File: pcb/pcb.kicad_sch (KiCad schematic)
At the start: 37 parts, among them J1 Ribbon Cable Header, J2 Ribbon Cable Header, J3 UPDI, SW1 MX Grey w/ LED, SW2 MX Grey w/ LED, SW3 1241.1100.7095, SW4 SW_SPST, U1 Display Driver, U2 Display Driver, U3 MCU, U4 OR, 2 Channels, U5 5V Buck Voltage Regulator, Y1 32.768 kHz

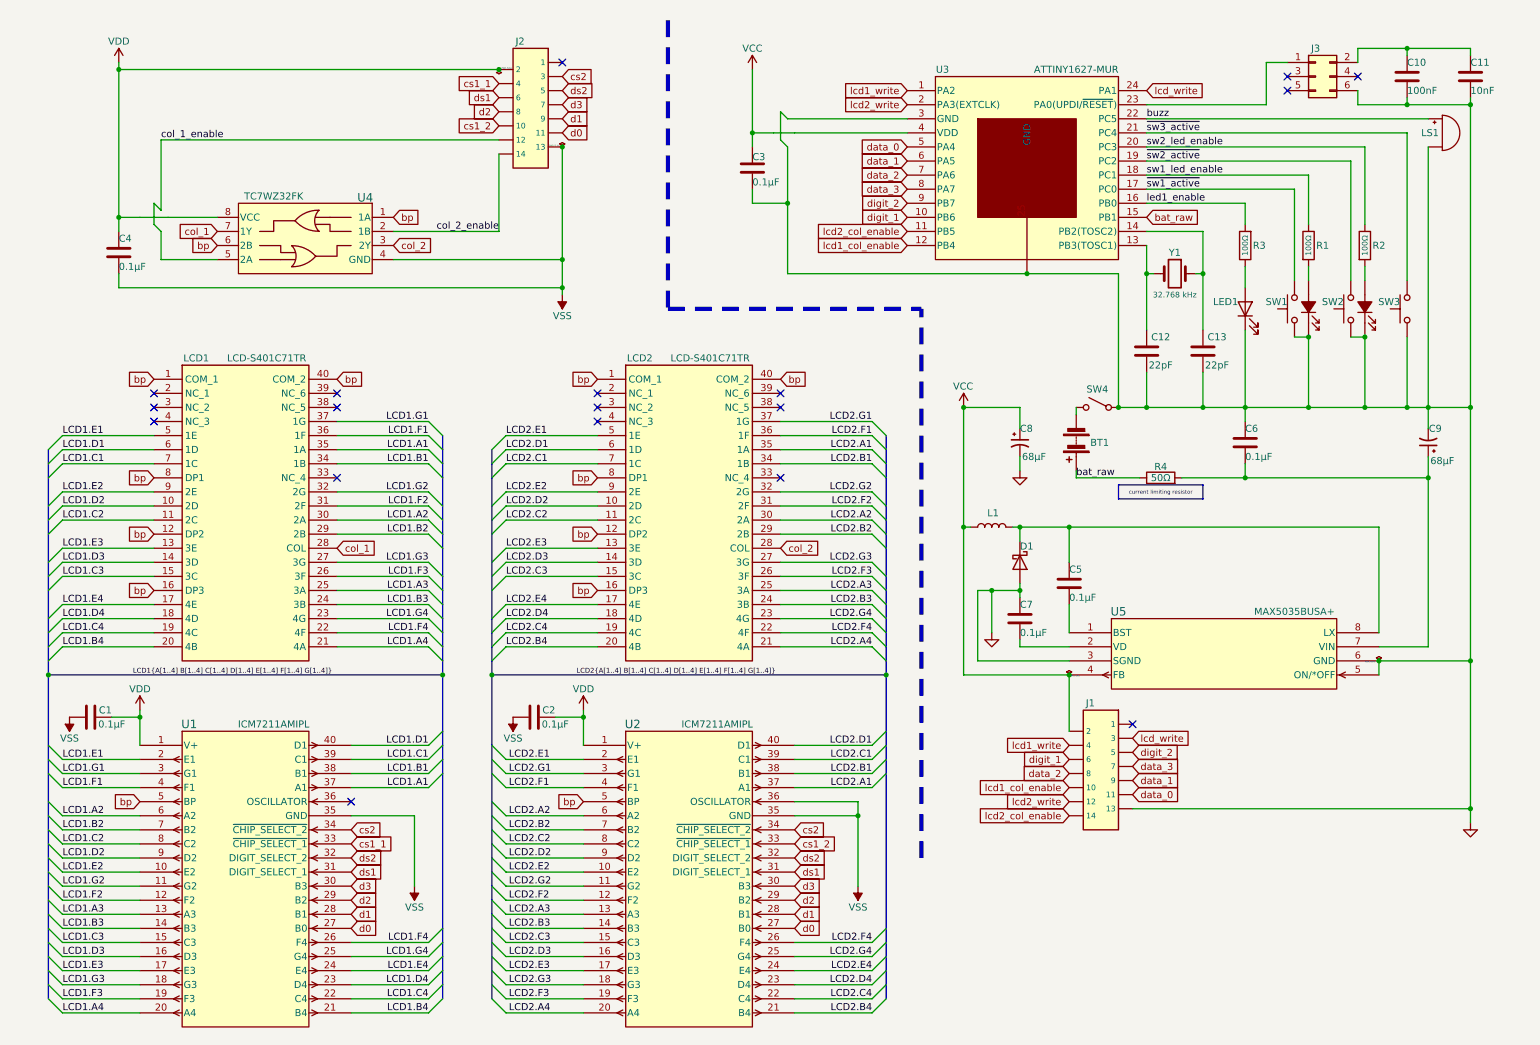
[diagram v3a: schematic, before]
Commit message: standardize cross-connector net names
Signed-off-by: Michael Darr <michael.e.darr@gmail.com>
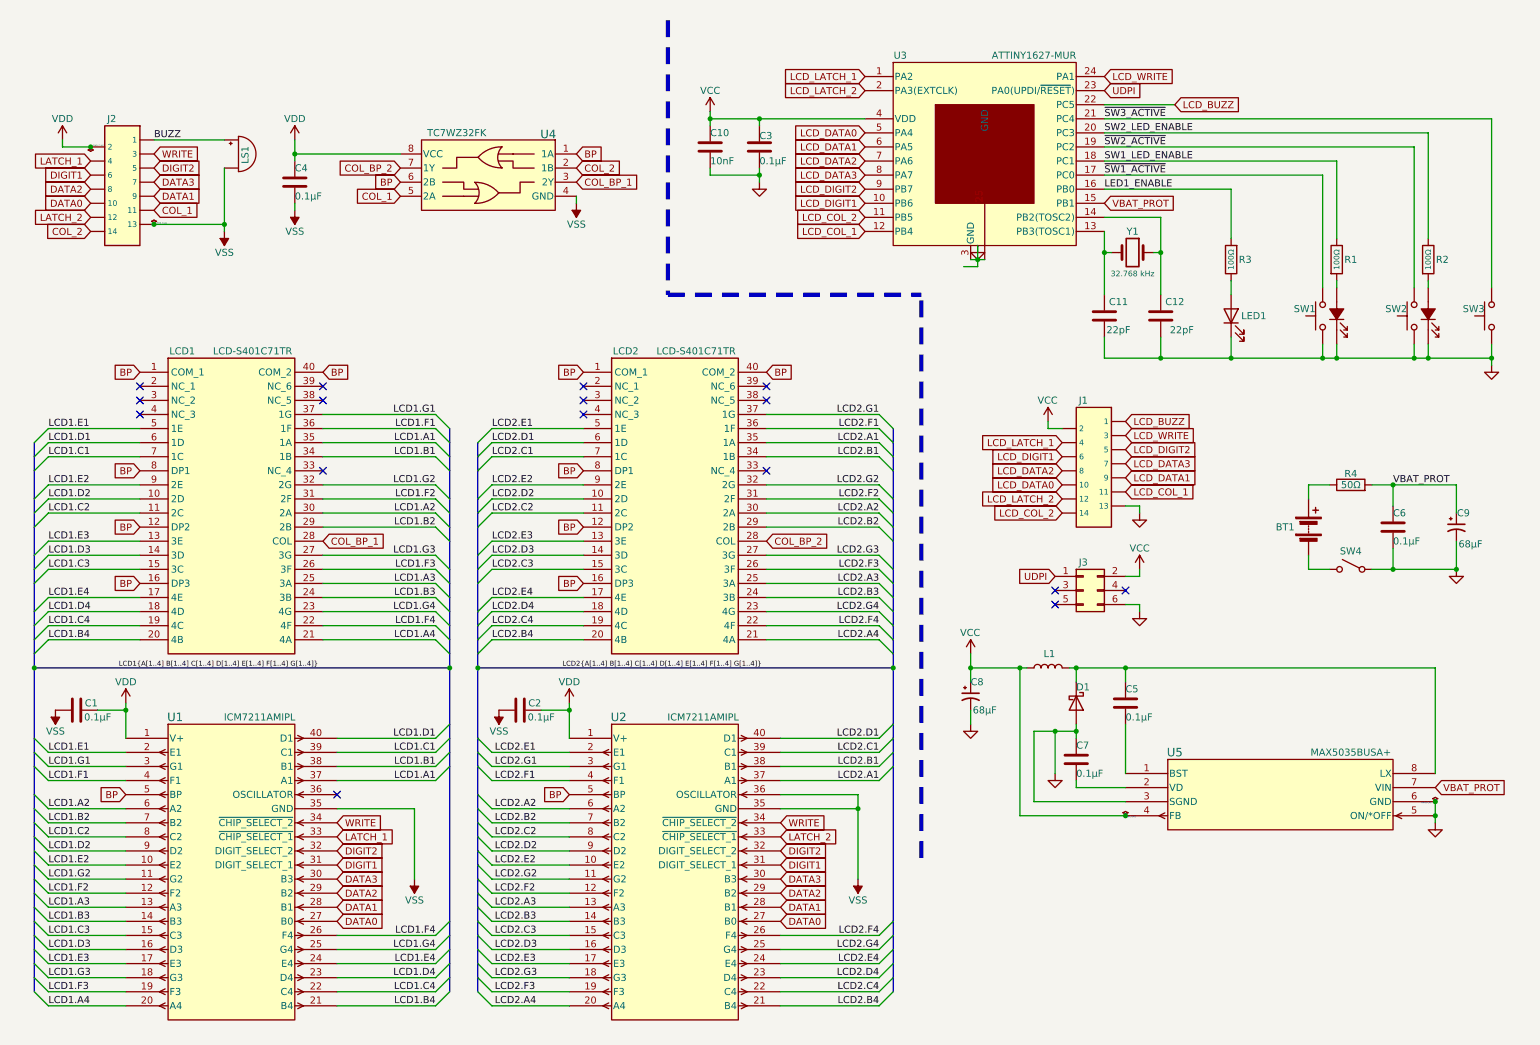
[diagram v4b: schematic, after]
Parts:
- removed C10: 100nF, Capacitor_SMD:C_0805_2012Metric_Pad1.18x1.45mm_HandSolder, symbol Device:C
- renumbered C11 to C10, C12 to C11, C13 to C12
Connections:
- net GND: now also C6.2; no longer C6.1, LS1.2 (+)
- net VCC: now also C10.1, J3.2 (Pin_2)
- net VSS: now also LS1.2 (+)
- net BUZZ: now reaches J2.1
- net BUZZ: now also LS1.1 (-)
- net UDPI: now reaches J3.1 (Pin_1), U3.23 (PA0(UPDI/~{RESET}))
- net LCD_BUZZ: now reaches J1.1
- net LCD_BUZZ: now also U3.22 (PC5)
- net VBAT_PROT: now reaches C9.1, R4.2, U5.7 (VIN)
- net VBAT_PROT: now also C6.1, U3.15 (PB1); no longer C6.2
- net bat_raw: no longer names the net of BT1.1 (+), R4.1
- net bat_raw: no longer U3.15 (PB1)
- net bp renamed BP
- removed net buzz: LS1.1 (-), U3.22 (PC5)
- net col_1 renamed COL_BP_1
- net COL_BP_1: now also U4.3 (2Y); no longer U4.7 (1Y)
- net col_1_enable renamed COL_1
- net COL_1: now also J2.11; no longer J2.12
- net col_2 renamed COL_BP_2
- net COL_BP_2: now also U4.7 (1Y); no longer U4.3 (2Y)
- net col_2_enable renamed COL_2
- net cs1_1 renamed LATCH_1
- net cs1_2 renamed DATA0
- net DATA0: now also U1.27 (B0), U2.27 (B0); no longer U2.33 (~{CHIP_SELECT_1})
- net cs2 renamed WRITE
- removed net d0: J2.11, U1.27 (B0), U2.27 (B0)
- net d1 renamed DATA1
- net d2 renamed DATA2
- net d3 renamed DATA3
- net data_0 renamed LCD_COL_1
- net LCD_COL_1: now also U3.12 (PB4); no longer U3.5 (PA4)
- net data_1 renamed LCD_DATA1
- net data_2 renamed LCD_DATA2
- net data_3 renamed LCD_DATA3
- net digit_1 renamed LCD_DIGIT1
- net digit_2 renamed LCD_DIGIT2
- net ds1 renamed DIGIT1
- net ds2 renamed DIGIT2
- net lcd1_col_enable renamed LCD_DATA0
- net LCD_DATA0: now also U3.5 (PA4); no longer U3.12 (PB4)
- net lcd1_write renamed LCD_LATCH_1
- net lcd2_col_enable renamed LCD_COL_2
- net lcd2_write renamed LCD_LATCH_2
- net lcd_write renamed LCD_WRITE
- net led1_enable renamed LED1_ENABLE
- net sw1_led_enable renamed SW1_LED_ENABLE
- net sw2_led_enable renamed SW2_LED_ENABLE
- net ~{sw1_active} renamed ~{SW1_ACTIVE}
- net ~{sw2_active} renamed ~{SW2_ACTIVE}
- net ~{sw3_active} renamed ~{SW3_ACTIVE}
- new net LATCH_2: J2.12, U2.33 (~{CHIP_SELECT_1})
- no-connect marks 18 -> 16
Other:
- moved on the sheet: BT1, C1, C10, C11, C12, C2, C3, C4, C5, C6, C7, C8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

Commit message: 0.2.0
Signed-off-by: Michael Darr <michael.e.darr@gmail.com>
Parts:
- removed C5: 0.1µF, Capacitor_SMD:C_0805_2012Metric_Pad1.18x1.45mm_HandSolder, symbol Device:C
- removed C9: 68µF, chess_clock:TPSD686K010R0100, symbol Device:C_Polarized_Small_US
- removed U5: 5V Buck Voltage Regulator, chess_clock:MAX5035BUSA+, symbol Clock-Parts:MAX5035BUSA+
- added U5: Voltage Regulator, chess_clock:MAX1836EUT50+T, symbol Clock-Parts:MAX1836EUT50+T
- BT1: footprint Connector_Wire:SolderWire-0.15sqmm_1x02_P4mm_D0.5mm_OD1.5mm -> chess_clock:BATTERY
- C6: renamed from C8; symbol Device:C_Polarized_Small_US -> Device:C_Polarized_US
- C7: value 0.1µF -> 10µF; PN CL21B104KBCNNNC -> CL21A106KOQNNNE
- C8: renamed from C10; PN (none) -> CL21B103KBANNNC
- renumbered C12 to C10, C6 to C5, C11 to C9
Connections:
- net GND: now also C7.2, J1.2, U5.1 (FB), U5.2 (GND); no longer C7.1, J1.13
- net LCD_BUZZ: now also J1.14; no longer J1.1
- net LCD_COL_1: now also J1.4; no longer J1.11
- net LCD_COL_2: now also J1.1; no longer J1.14
- net LCD_DATA0: now also J1.5; no longer J1.10
- net LCD_DATA1: now also J1.6; no longer J1.9
- net LCD_DATA2: now also J1.7; no longer J1.8
- net LCD_DATA3: now also J1.8; no longer J1.7
- net LCD_DIGIT1: now also J1.9; no longer J1.6
- net LCD_DIGIT2: now also J1.10; no longer J1.5
- net LCD_LATCH_1: now also J1.11; no longer J1.4
- net LCD_LATCH_2: now also J1.3; no longer J1.12
- net LCD_WRITE: now also J1.12; no longer J1.3
- net VBAT_PROT: now also C7.1, U5.3 (IN), U5.5 (~{SHDN}); no longer C5.1
- net VCC: now also C5.1, J1.13, U5.6 (OUT); no longer J1.2
- net at D1.1 (K), L1.2: now also U5.4 (LX)
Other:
- moved on the sheet: BT1, C5, C6, D1, J1, J3, L1, R1, R2, R3, R4, SW1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

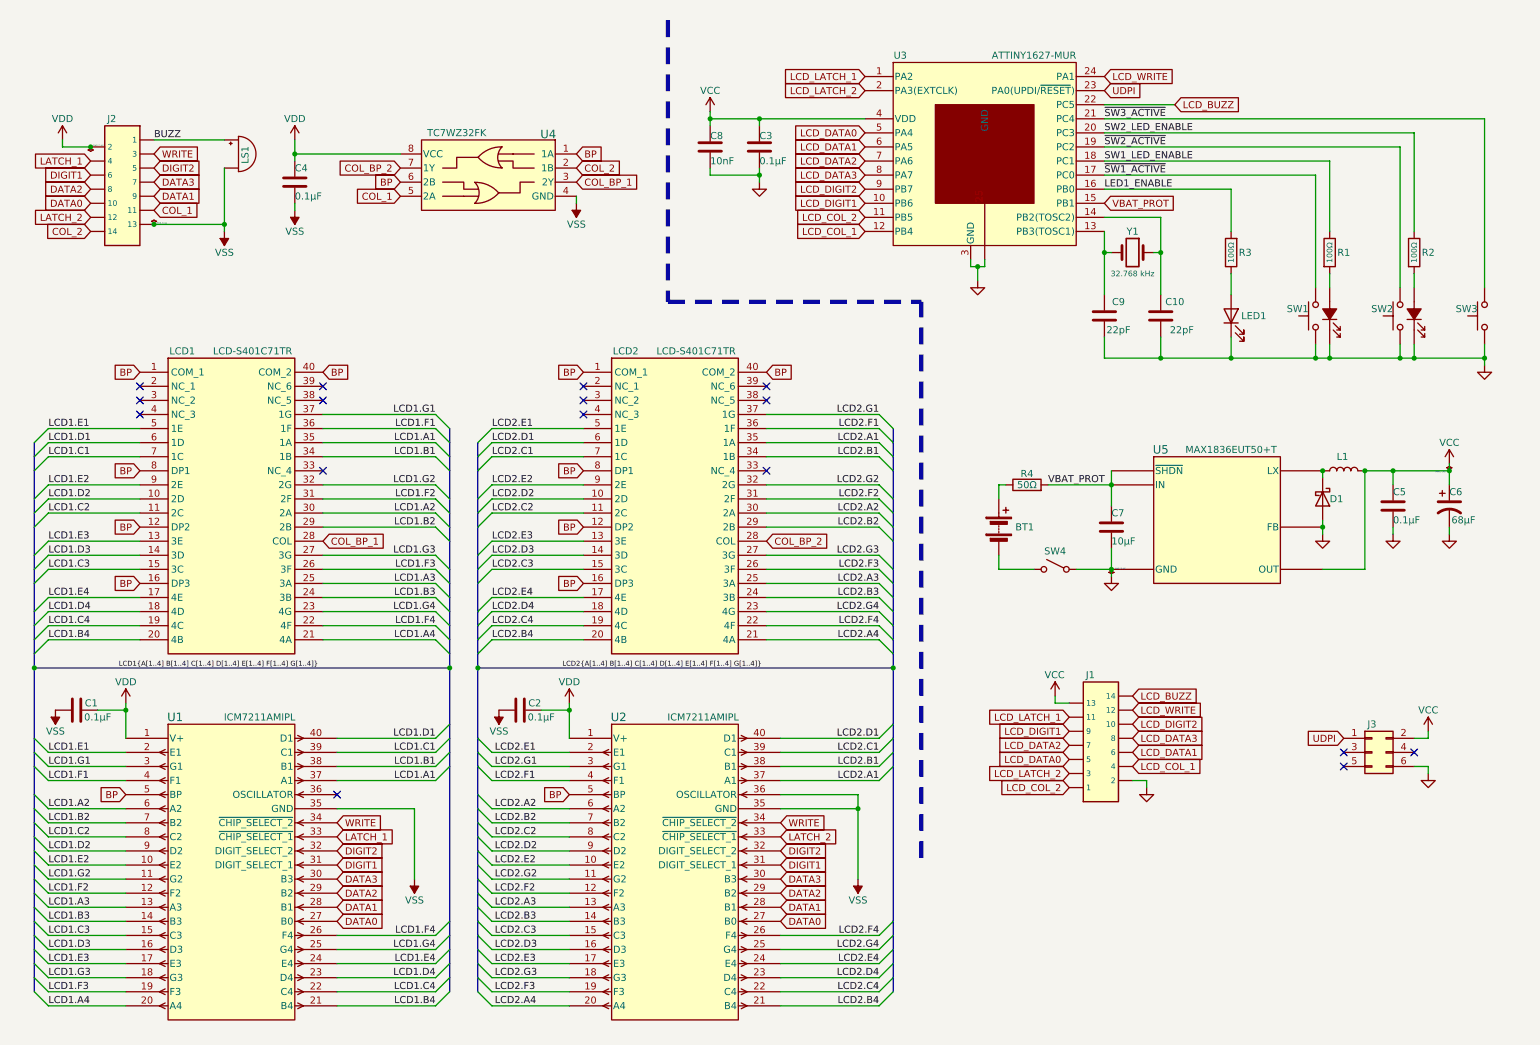
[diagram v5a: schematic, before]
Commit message: Move micro onto LCD board
Signed-off-by: Michael Darr <michael.e.darr@gmail.com>
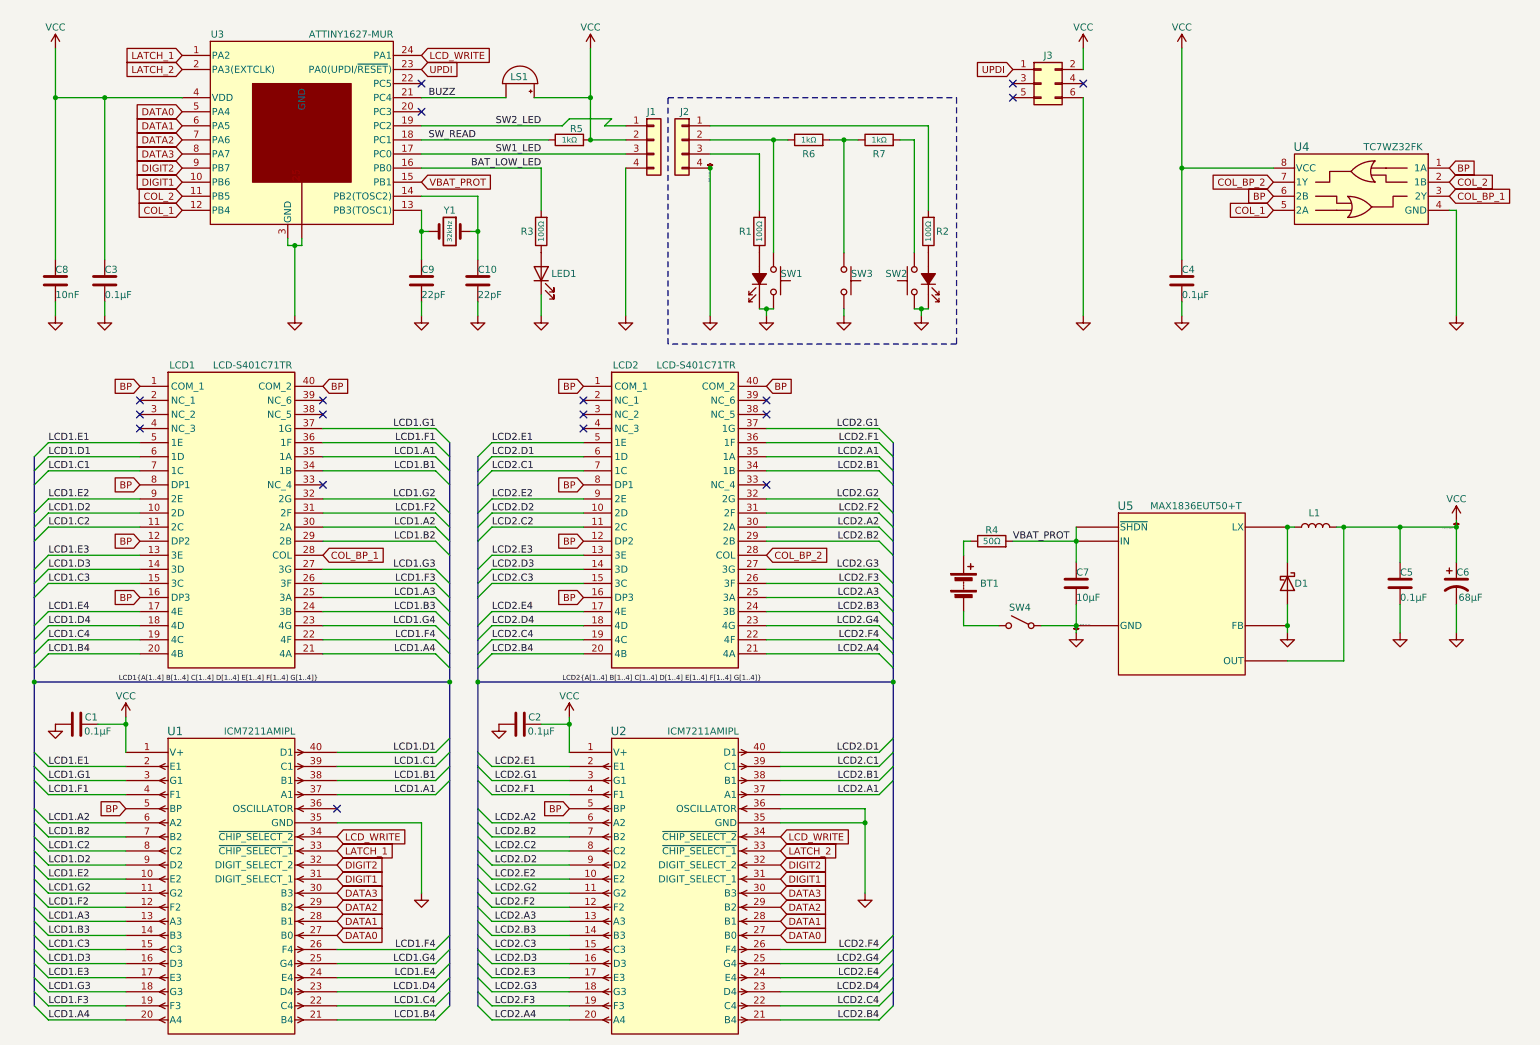
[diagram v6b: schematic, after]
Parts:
- removed J1, J2: Ribbon Cable Header, chess_clock:903250014, symbol Clock-Parts:903250014
- added J1, J2: Conn_01x04, symbol Connector_Generic:Conn_01x04
- added R5, R6, R7: 1kΩ, symbol Device:R
- L1: value 100μH -> 47μH; footprint chess_clock:DO5022P-104MLD -> chess_clock:Inductor_6060; PN DO5022P-104MLD -> HPC 6045NV-470M
- Y1: value 32.768 kHz -> 32kHz
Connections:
- net LCD_COL_1 is gone; now on net COL_1: U3.12 (PB4)
- net LCD_COL_2 is gone; now on net COL_2: U3.11 (PB5)
- net LCD_DATA0 is gone; now on net DATA0: U3.5 (PA4)
- net LCD_DATA1 is gone; now on net DATA1: U3.6 (PA5)
- net LCD_DATA2 is gone; now on net DATA2: U3.7 (PA6)
- net LCD_DATA3 is gone; now on net DATA3: U3.8 (PA7)
- net LCD_DIGIT1 is gone; now on net DIGIT1: U3.10 (PB6)
- net LCD_DIGIT2 is gone; now on net DIGIT2: U3.9 (PB7)
- net LCD_LATCH_1 is gone; now on net LATCH_1: U3.1 (PA2)
- net LCD_LATCH_2 is gone; now on net LATCH_2: U3.2 (PA3(EXTCLK))
- net VDD is gone; now on net VCC: C1.2, C2.2, C4.1, U1.1 (V+), U2.1 (V+), U4.8 (VCC)
- net WRITE is gone; now on net LCD_WRITE: U1.34 (~{CHIP_SELECT_2}), U2.34 (~{CHIP_SELECT_2})
- net BUZZ: now also LS1.2 (+), U3.21 (PC4); no longer LS1.1 (-)
- net GND: now also C1.1, C2.1, C4.2, U1.35 (GND), U2.35 (GND), U2.36 (OSCILLATOR), U4.4 (GND), J1.4 (Pin_4); no longer SW1.1, SW1.3 (K), SW2.1, SW2.3 (K), SW3.1
- net VCC: now also LS1.1 (-), J1.2 (Pin_2), R5.2
- net at SW1.4 (A): now also R1.1; no longer R1.2
- net at SW2.4 (A): now also R2.1; no longer R2.2
- net LCD_BUZZ: no longer names the net of U3.22 (PC5)
- net LED1_ENABLE renamed BAT_LOW_LED
- net SW1_LED_ENABLE renamed SW_READ
- net SW_READ: now also R5.1; no longer R1.1
- net SW2_LED_ENABLE: no longer names the net of U3.20 (PC3)
- net SW2_LED_ENABLE: no longer R2.1
- net UDPI renamed UPDI
- removed net VSS: C1.1, C2.1, C4.2, LS1.2 (+), U1.35 (GND), U2.35 (GND), U2.36 (OSCILLATOR), U4.4 (GND)
- net ~{SW1_ACTIVE}: no longer names the net of SW1.2
- net ~{SW1_ACTIVE}: now also J2.2 (Pin_2), R6.1; no longer U3.17 (PC0)
- net ~{SW2_ACTIVE}: no longer names the net of SW2.2
- net ~{SW2_ACTIVE}: now also R7.2; no longer U3.19 (PC2)
- net ~{SW3_ACTIVE} renamed GND1
- net GND1: now also SW1.1, SW1.3 (K), SW2.1, SW2.3 (K), J2.4 (Pin_4); no longer U3.21 (PC4)
- new net: R6.2, R7.1, SW3.1
- new net: J2.1 (Pin_1), R2.2
- new net: J2.3 (Pin_3), R1.2
- new net SW1_LED: J1.3 (Pin_3), U3.17 (PC0)
- new net SW2_LED: J1.1 (Pin_1), U3.19 (PC2)
- no-connect marks 16 -> 18
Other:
- moved on the sheet: BT1, C1, C10, C2, C3, C4, C5, C6, C7, C8, C9, D1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

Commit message: back up pcb work
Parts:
- removed SW4: SW_SPST, chess_clock:CWSA11AAN1H, symbol Switch:SW_SPST
- added R8: 2.7kΩ, symbol Device:R
- R5: value 1kΩ -> 2.7kΩ
- R6: value 1kΩ -> 27kΩ
- R7: value 1kΩ -> 12kΩ
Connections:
- net GND: now also BT1.2 (-)
- net at R6.1, SW1.2: no longer J2.2 (Pin_2)
- net at R7.1, SW3.1: no longer R6.2
- net at R7.2: now also J2.2 (Pin_2), R6.2, R8.1; no longer SW2.2
- new net: R8.2, SW2.2
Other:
- moved on the sheet: R6, R7

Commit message: Redo pcb layout
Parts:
- removed R4: 50Ω, chess_clock:352151RFT, symbol Device:R
- J1, J2: footprint (none) -> chess_clock:2005290040; symbol Connector_Generic:Conn_01x04 -> Clock-Parts:200529-0040; Height (none) -> 2; Manufacturer_Name (none) -> Molex; Manufacturer_Part_Number (none) -> 200529-0040; Mouser Part Number (none) -> 538-200529-0040; Mouser Price/Stock (none) -> https://www.mouser.co.uk/ProductDetail/Molex/200529-0040?qs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
- R4: renamed from R8; footprint (none) -> Resistor_SMD:R_0805_2012Metric_Pad1.20x1.40mm_HandSolder
- R5, R6, R7: footprint (none) -> Resistor_SMD:R_0805_2012Metric_Pad1.20x1.40mm_HandSolder
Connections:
- net VBAT_PROT is gone; now on net VBAT: C7.1, U3.15 (PB1), U5.3 (IN), U5.5 (~{SHDN})
- net GND: now also J1.5, J1.6
- net GND1: now also J2.5, J2.6
- net VBAT: now reaches BT1.1 (+)
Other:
- moved on the sheet: BT1
